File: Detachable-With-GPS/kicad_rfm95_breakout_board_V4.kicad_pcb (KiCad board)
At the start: 2 copper layers, 61 x 65.5 mm, 55 parts, among them J1 USB_B_Micro, J2 Conn_Coaxial, J3 Male Pinheader 1x20, J4 Male Pinheader 1x20, J5 Male Pinheader 1x2, J6 ARM 10pin, SW1 SW_Push, SW2 SW_Push, SW3 SW_Push, SW4 SW_Push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

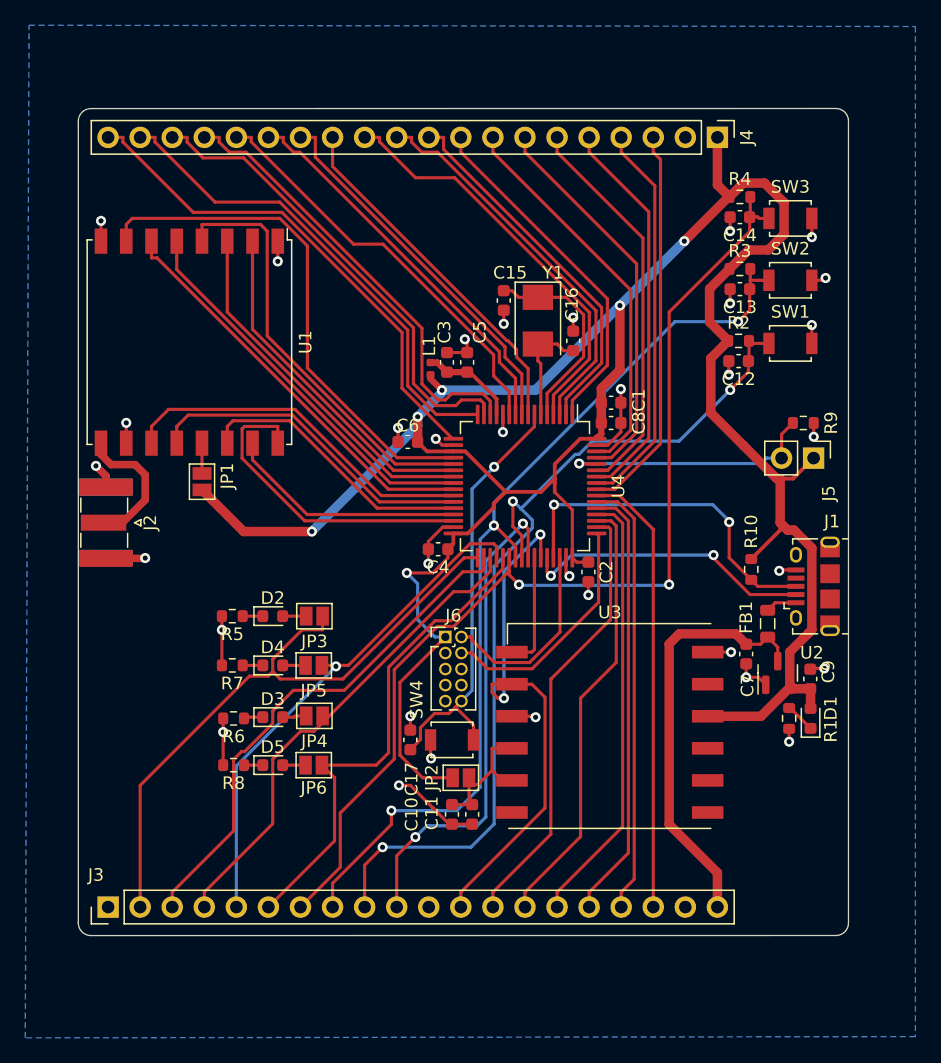
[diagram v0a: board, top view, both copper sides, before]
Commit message: Update USB Pullup (R already internal in STM32L0 processors)
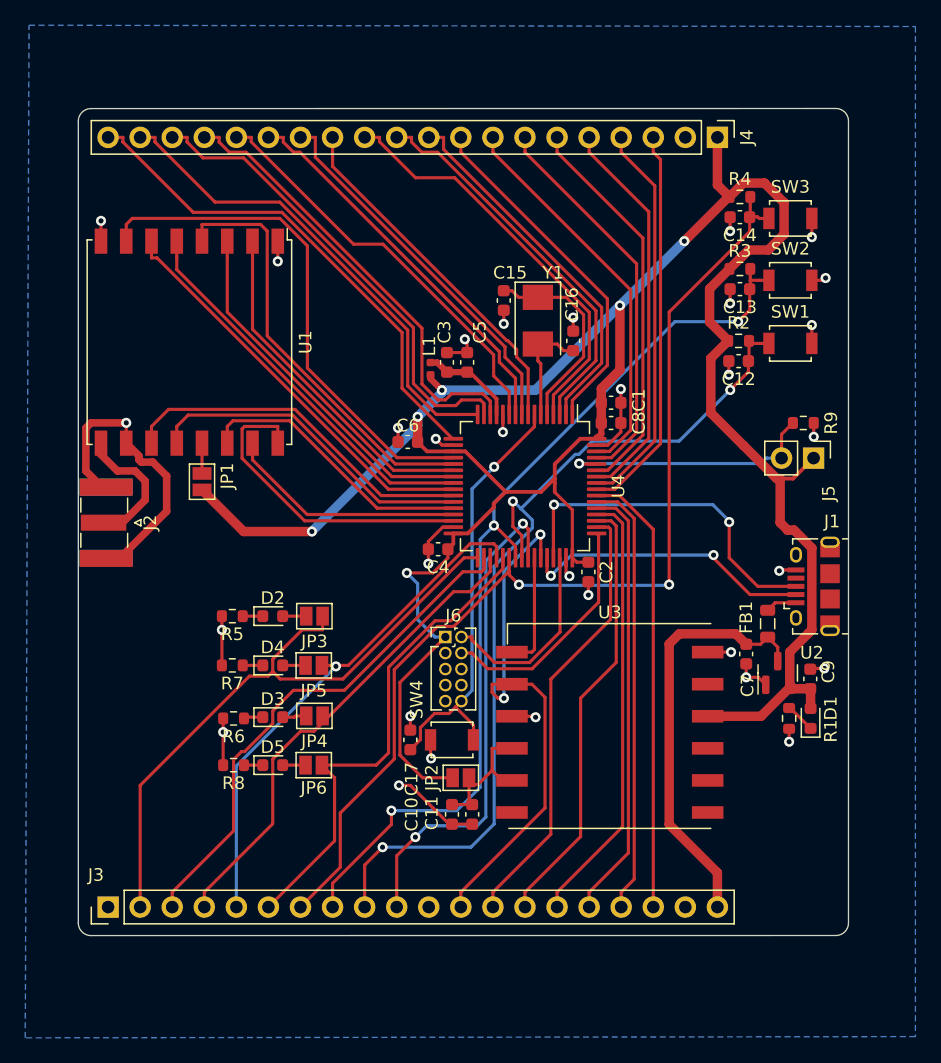
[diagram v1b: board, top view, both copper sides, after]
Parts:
- removed R10: 1k5, Resistor_SMD:R_0603_1608Metric
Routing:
- net GND: track 67.4 -> 84.8 mm, vias 33 -> 31
- net +3.3V: track 206.6 -> 202.2 mm
